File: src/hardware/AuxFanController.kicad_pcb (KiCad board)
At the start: 2 copper layers, 26 x 20 mm, 12 parts, among them J1 MC 1,5/2, J1' MCV 1,5/2, J2 Fan 1, J3 Fan 2, J4 Fan 3, U1 12F1501, U2 MCP9701A

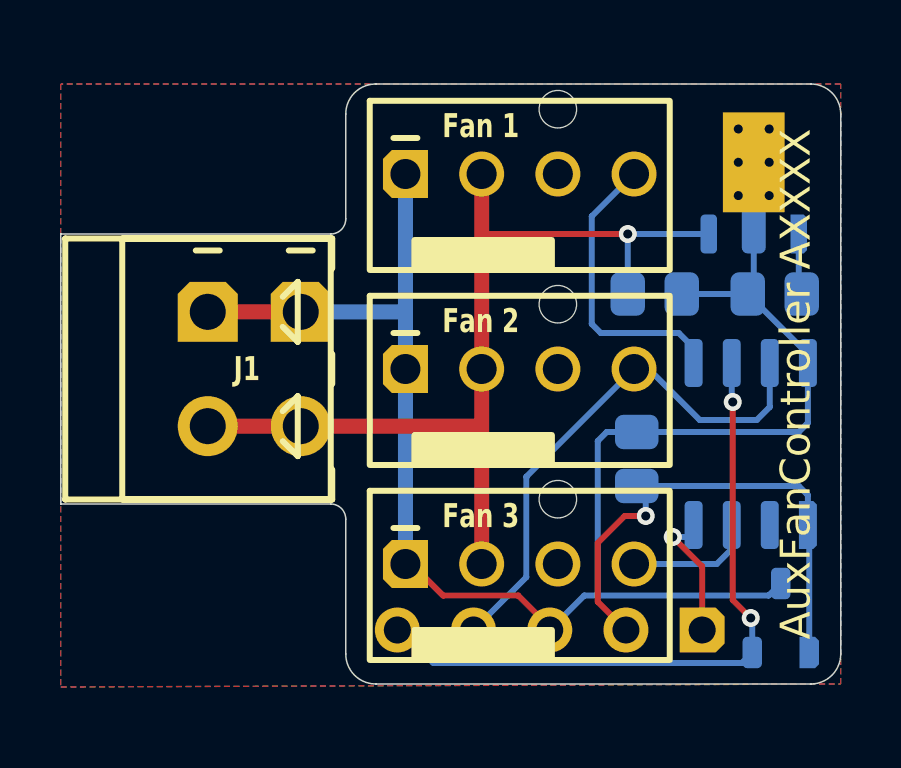
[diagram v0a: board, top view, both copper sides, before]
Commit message: Updated board refdes
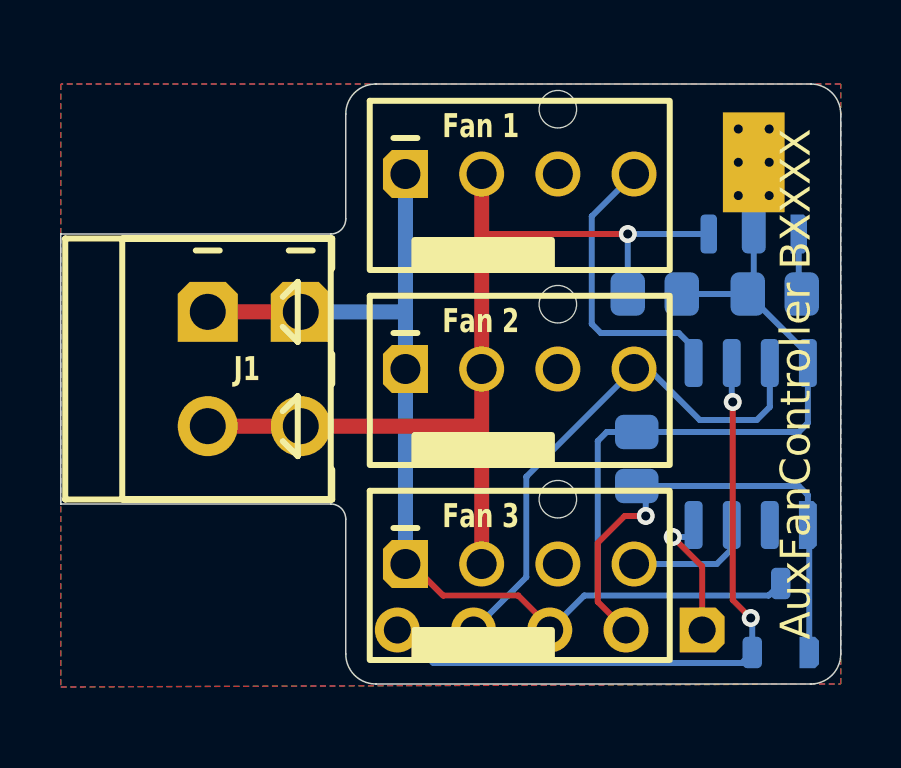
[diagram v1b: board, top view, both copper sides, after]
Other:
- board text added: "AuxFanController BXXXX"
- board text removed: "AuxFanController AXXXX"
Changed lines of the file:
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@@
 		(layer "Edge.Cuts")
 	)
-	(gr_text "AuxFanController AXXXX"
+	(gr_text "AuxFanController BXXXX"
 		(at 39.5 25 90)
 		(layer "F.SilkS")

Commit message: Cleanup
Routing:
- net +5V: track 18.8 -> 26.8 mm, vias 1 -> 3
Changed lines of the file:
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@@
 		(descr "Molex 047053-1000")
 		(property "Reference" "J2"
-			(at -3.8 -1.8 180)
+			(at 2.95 -1.75 180)
 			(layer "F.Fab")
 			(effects
@@
 		)
 		(attr through_hole)
-		(fp_line
-			(start -4.21 -1.2)
-			(end -3.41 -1.2)
+		(fp_rect
+			(start -5 -2.44)
+			(end 5 3.2)
 			(stroke
 				(width 0.2)
 				(type default)
 			)
+			(fill no)
 			(layer "F.SilkS")
 		)
 		(fp_rect
-			(start -5 -2.44)
-			(end 5 3.2)
+			(start -4.21 -2.44)
+			(end -3.41 -2.04)
 			(stroke
 				(width 0.2)
-				(type default)
+				(type solid)
 			)
-			(fill no)
+			(fill yes)
 			(layer "F.SilkS")
 		)
@@
 		(attr through_hole)
 		(fp_line
-			(start -3.95 -0.4)
-			(end -3.95 0.4)
-			(stroke
-				(width 0.2)
-				(type default)
-			)
-			(layer "F.SilkS")
-		)
-		(fp_line
 			(start -2.905 -3)
 			(end -2.405 -2.5)
@@
 		)
 		(fp_rect
+			(start -4.35 -0.4)
+			(end -3.95 0.4)
+			(stroke
+				(width 0.2)
+				(type solid)
+			)
+			(fill yes)
+			(layer "F.SilkS")
+		)
+		(fp_rect
 			(start -4.35 -4.1)
 			(end 4.35 2.85)
@@
 		(embedded_fonts no)
 		(model "${KICAD8_3DMODEL_DIR}/Connector_Phoenix_MC.3dshapes/PhoenixContact_MCV_1,5_2-G-3.81_1x02_P3.81mm_Vertical.wrl"
-			(hide yes)
 			(offset
 				(xyz -1.905 0 0)
@@
 		(descr "Molex 047053-1000")
 		(property "Reference" "J4"
-			(at -3.8 -1.8 180)
+			(at 3 -1.65 180)
 			(layer "F.Fab")
 			(effects
@@
 		)
 		(attr through_hole)
-		(fp_line
-			(start -4.21 -1.2)
-			(end -3.41 -1.2)
+		(fp_rect
+			(start -5 -2.44)
+			(end 5 3.2)
 			(stroke
 				(width 0.2)
 				(type default)
 			)
+			(fill no)
 			(layer "F.SilkS")
 		)
 		(fp_rect
-			(start -5 -2.44)
-			(end 5 3.2)
+			(start -4.21 -2.44)
+			(end -3.41 -2.04)
 			(stroke
 				(width 0.2)
-				(type default)
+				(type solid)
 			)
-			(fill no)
+			(fill yes)
 			(layer "F.SilkS")
 		)
@@
 		)
 		(fp_line
-			(start -3.95 -0.4)
-			(end -3.95 0.4)
-			(stroke
-				(width 0.2)
-				(type default)
-			)
-			(layer "F.SilkS")
-		)
-		(fp_line
 			(start -4.35 -1.05)
 			(end -4.35 7.85)
@@
 		)
 		(fp_rect
+			(start -4.35 -0.4)
+			(end -3.95 0.4)
+			(stroke
+				(width 0.2)
+				(type solid)
+			)
+			(fill yes)
+			(layer "F.SilkS")
+		)
+		(fp_rect
 			(start -4.605 -1.7)
 			(end 4.605 8)
@@
 		(descr "Molex 047053-1000")
 		(property "Reference" "J3"
-			(at -3.8 -1.8 180)
+			(at 3 -1.7 180)
 			(layer "F.Fab")
 			(effects
@@
 		)
 		(attr through_hole)
-		(fp_line
-			(start -4.21 -1.2)
-			(end -3.41 -1.2)
+		(fp_rect
+			(start -5 -2.44)
+			(end 5 3.2)
 			(stroke
 				(width 0.2)
 				(type default)
 			)
+			(fill no)
 			(layer "F.SilkS")
 		)
 		(fp_rect
-			(start -5 -2.44)
-			(end 5 3.2)
+			(start -4.21 -2.44)
+			(end -3.41 -2.04)
 			(stroke
 				(width 0.2)
-				(type default)
+				(type solid)
 			)
-			(fill no)
+			(fill yes)
 			(layer "F.SilkS")
 		)
@@
 			)
 		)
-		(attr smd)
+		(attr through_hole)
 		(fp_line
-			(start -3.81 0.2)
-			(end -3.81 -0.2)
+			(start -3.81 0.4)
+			(end -3.81 -0.4)
 			(stroke
 				(width 0.2)
-				(type default)
+				(type solid)
 			)
 			(layer "B.SilkS")
@@
 			(layer "B.SilkS")
 		)
+		(fp_rect
+			(start -6.45 1.37)
+			(end 6.45 -1.37)
+			(stroke
+				(width 0.01)
+				(type dash)
+			)
+			(fill no)
+			(layer "B.CrtYd")
+		)
 		(fp_text user "GND"
 			(at 0 0.9 0)
@@
 		)
 		(attr smd)
-		(fp_line
-			(start -0.4 1.9)
+		(fp_rect
+			(start -0.4 2.3)
 			(end 0.4 1.9)
 			(stroke
 				(width 0.2)
-				(type default)
+				(type solid)
 			)
+			(fill yes)
 			(layer "B.SilkS")
 		)
@@
 		(descr "AS78L05RTR-E1")
 		(property "Reference" "VR1"
-			(at 1.8 3.7 90)
+			(at 0 4.7 0)
 			(layer "B.SilkS")
 			(effects
@@
 			)
 		)
-		(attr smd)
 		(fp_line
 			(start 2.05 2.65)
@@
 		)
 		(fp_line
-			(start -1.3 0.95)
-			(end -1.7 0.95)
-			(stroke
-				(width 0.2)
-				(type default)
-			)
-			(layer "B.SilkS")
-		)
-		(fp_line
 			(start -2.05 2.65)
 			(end -1.1 2.65)
@@
 	)
 	(segment
+		(start 39.9 28.4)
+		(end 39.9 21.3)
+		(width 0.2)
+		(layer "F.Cu")
+		(net 9)
+	)
+	(segment
+		(start 39.9 21.3)
+		(end 39.6 21)
+		(width 0.2)
+		(layer "F.Cu")
+		(net 9)
+	)
+	(segment
 		(start 32.9 32.26)
 		(end 32.9 30.3)
@@
 		(net 9)
 	)
+	(via
+		(at 39.6 21)
+		(size 0.6)
+		(drill 0.3)
+		(layers "F.Cu" "B.Cu")
+		(net 9)
+	)
+	(via
+		(at 39.9 28.4)
+		(size 0.6)
+		(drill 0.3)
+		(layers "F.Cu" "B.Cu")
+		(net 9)
+	)
 	(segment
-		(start 39.6 28.4)
-		(end 39.905 28.705)
+		(start 39.905 28.405)
+		(end 39.9 28.4)
 		(width 0.2)
 		(layer "B.Cu")
@@
 	)
 	(segment
-		(start 34.5 28.4)
-		(end 39.6 28.4)
+		(start 34.5 29.4)
+		(end 34.5 28.4)
 		(width 0.2)
 		(layer "B.Cu")
@@
 	)
 	(segment
-		(start 34.5 28.4)
-		(end 34.5 29.4)
+		(start 34.2 28.4)
+		(end 39.9 28.4)
 		(width 0.2)
 		(layer "B.Cu")
@@
 	)
 	(segment
-		(start 39.95 33.95)
-		(end 39.95 29.745)
+		(start 39.905 29.7)
+		(end 39.905 28.405)
 		(width 0.2)
 		(layer "B.Cu")
@@
 	)
 	(segment
-		(start 39.6 20)
-		(end 39.6 21.9)
+		(start 39.95 33.95)
+		(end 39.95 29.745)
 		(width 0.2)
 		(layer "B.Cu")
@@
 	)
 	(segment
-		(start 39.905 28.705)
-		(end 39.905 29.7)
+		(start 39.6 20)
+		(end 39.6 21.9)
 		(width 0.2)
 		(layer "B.Cu")
